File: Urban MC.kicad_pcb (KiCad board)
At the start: 4 copper layers, 166.4 x 125.1 mm, 78 parts, among them J1 Conn_01x02, J2 Conn_01x02, J3 Conn_01x03, J4 Conn_01x02, Q1 IQE022N06LM5CGSCATMA1, Q10 IQE022N06LM5CGSCATMA1, Q11 IQE022N06LM5CGSCATMA1, Q12 IQE022N06LM5CGSCATMA1, Q13 IQE022N06LM5CGSCATMA1, Q14 IQE022N06LM5CGSCATMA1, Q15 IQE022N06LM5CGSCATMA1, Q16 IQE022N06LM5CGSCATMA1, Q17 IQE022N06LM5CGSCATMA1, Q18 IQE022N06LM5CGSCATMA1, Q19 IQE022N06LM5CGSCATMA1, Q2 IQE022N06LM5CGSCATMA1, Q20 IQE022N06LM5CGSCATMA1, Q21 IQE022N06LM5CGSCATMA1, Q22 IQE022N06LM5CGSCATMA1, Q23 IQE022N06LM5CGSCATMA1, Q24 IQE022N06LM5CGSCATMA1, Q3 IQE022N06LM5CGSCATMA1, Q4 IQE022N06LM5CGSCATMA1, Q5 IQE022N06LM5CGSCATMA1, Q6 IQE022N06LM5CGSCATMA1, Q7 IQE022N06LM5CGSCATMA1, Q8 IQE022N06LM5CGSCATMA1, Q9 IQE022N06LM5CGSCATMA1, SW1 CAN_TERM, SW2 SW_Push, U1 MCP2561/2, U2 MCP4725, U3 MCP2515-xSO, Y1 8MHz

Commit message: post design review
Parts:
- moved C10 0.26 mm to (206.0, 89.9)
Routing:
- net GND: track 221.0 -> 179.9 mm, vias 94 -> 92
- net +12V: track 140.8 -> 100.8 mm, vias 2 -> 3
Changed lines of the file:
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@@
 	(footprint "Capacitor_SMD:C_2220_5750Metric"
 		(layer "F.Cu")
-		(at 205.994 90.18 90)
+		(at 205.994 89.916 90)
 		(descr "Capacitor SMD 2220 (5750 Metric), square (rectangular) end terminal, IPC-7351 nominal, (Body size from: http://datasheets.avx.com/AVX-HV_MLCC.pdf), generated with kicad-footprint-generator")
 		(tags "capacitor")
@@
 	)
 	(segment
-		(start 130.81 91.44)
-		(end 128.778 89.408)
-		(width 0.25)
-		(layer "F.Cu")
-		(net 7)
-	)
-	(segment
 		(start 131.572 65.532)
 		(end 132.08 65.532)
@@
 	)
 	(segment
-		(start 132.588 92.964)
-		(end 134.112 92.964)
-		(width 0.25)
-		(layer "F.Cu")
-		(net 7)
-	)
-	(segment
 		(start 121.266474 62.738)
 		(end 121.744737 62.259737)
@@
 	)
 	(segment
-		(start 134.112 92.964)
-		(end 135.382 94.234)
-		(width 0.25)
-		(layer "F.Cu")
-		(net 7)
-	)
-	(segment
 		(start 120.7825 77.47)
 		(end 121.719092 77.47)
@@
 	)
 	(segment
-		(start 128.778 89.408)
-		(end 128.778 79.502)
-		(width 0.25)
-		(layer "F.Cu")
-		(net 7)
-	)
-	(segment
 		(start 153.416 54.102)
 		(end 155.057 52.461)
@@
 	)
 	(via
-		(at 128.778 79.502)
-		(size 0.8)
-		(drill 0.4)
-		(layers "F.Cu" "B.Cu")
-		(net 7)
-	)
-	(via
 		(at 222.504 56.642)
 		(size 0.8)
@@
 	)
 	(via
-		(at 135.382 94.234)
-		(size 0.8)
-		(drill 0.4)
-		(layers "F.Cu" "B.Cu")
-		(net 7)
-	)
-	(via
 		(at 221.742 129.032)
 		(size 0.8)
@@
 	)
 	(segment
-		(start 128.778 79.502)
-		(end 128.27 78.994)
-		(width 0.25)
-		(layer "B.Cu")
-		(net 7)
-	)
-	(segment
 		(start 141.988792 125.476)
 		(end 154.94 125.476)
@@
 	)
 	(segment
-		(start 151.892 94.234)
-		(end 156.718 89.408)
-		(width 0.25)
-		(layer "B.Cu")
-		(net 7)
-	)
-	(segment
 		(start 154.94 125.476)
 		(end 155.702 126.238)
@@
 	)
 	(segment
-		(start 128.27 78.994)
-		(end 127.254 78.994)
-		(width 0.25)
-		(layer "B.Cu")
-		(net 7)
-	)
-	(segment
 		(start 124.9895 65.8075)
 		(end 124.9895 63.7755)
@@
 	)
 	(segment
-		(start 135.382 94.234)
-		(end 151.892 94.234)
-		(width 0.25)
-		(layer "B.Cu")
-		(net 7)
-	)
-	(segment
 		(start 124.9895 63.7755)
 		(end 123.444 62.23)
@@
 	)
 	(via
-		(at 153.924 122.174)
+		(at 134.112 88.9)
 		(size 0.8)
 		(drill 0.4)
@@
 		(net 21)
 	)
-	(segment
-		(start 139.192 88.9)
-		(end 141.224 90.932)
-		(width 1.34)
-		(layer "In2.Cu")
-		(net 21)
-	)
-	(segment
-		(start 141.224 90.932)
-		(end 141.224 120.414052)
-		(width 1.34)
-		(layer "In2.Cu")
+	(via
+		(at 153.924 122.174)
+		(size 0.8)
+		(drill 0.4)
+		(layers "F.Cu" "B.Cu")
 		(net 21)
 	)
@@
 	)
 	(segment
-		(start 144.253948 123.444)
-		(end 152.654 123.444)
+		(start 134.112 88.9)
+		(end 139.192 88.9)
 		(width 1.34)
 		(layer "In2.Cu")
@@
 	)
 	(segment
-		(start 141.224 120.414052)
-		(end 144.253948 123.444)
+		(start 144.253948 123.444)
+		(end 152.654 123.444)
 		(width 1.34)
 		(layer "In2.Cu")
@@
 	)
 	(segment
-		(start 130.81 88.9)
-		(end 139.192 88.9)
-		(width 1.34)
-		(layer "In2.Cu")
-		(net 21)
-	)
-	(segment
 		(start 153.416 88.9)
 		(end 154.432 87.884)
@@
 		(polygon
 			(pts
-				(xy 171.972957 71.891994) (xy 239.536957 72.145994) (xy 239.536957 79.003994) (xy 259.073585 79.003994)
-				(xy 259.073585 93.989994) (xy 239.790957 93.989994) (xy 239.790957 87.701768) (xy 209.162714 87.701768)
-				(xy 209.162714 88.336768) (xy 171.97264 88.299721) (xy 171.941329 83.243024)
+				(xy 171.958 71.882) (xy 239.522 71.882) (xy 239.536957 79.003994) (xy 259.073585 78.994) (xy 259.073585 93.989994)
+				(xy 239.790957 93.989994) (xy 239.790957 87.701768) (xy 209.162714 87.701768) (xy 209.162714 88.336768)
+				(xy 171.97264 88.299721) (xy 171.941329 83.243024)
 			)
 		)
@@
 		(polygon
 			(pts
-				(xy 170.942 90.424) (xy 199.644 90.424) (xy 199.644 106.172) (xy 167.132 106.172) (xy 167.132 112.268)
-				(xy 152.4 112.268) (xy 152.146 134.62) (xy 169.672 134.62) (xy 169.672 127) (xy 199.898 127) (xy 199.898 142.494)
+				(xy 170.942 90.424) (xy 199.644 90.424) (xy 199.644 106.172) (xy 170.434 106.172) (xy 170.434 112.268)
+				(xy 152.4 112.268) (xy 152.4 134.62) (xy 169.672 134.62) (xy 169.672 127) (xy 199.898 127) (xy 199.898 142.494)
 				(xy 240.538 142.494) (xy 240.538 136.652) (xy 259.08 136.652) (xy 259.08 153.67) (xy 136.435317 153.67)
 				(xy 136.525 59.944) (xy 171.45 59.944) (xy 171.45 54.61) (xy 199.898 54.61) (xy 199.898 71.12) (xy 171.196 71.12)
@@
 		(polygon
 			(pts
-				(xy 200.914 89.662) (xy 213.049576 89.684724) (xy 213.042396 88.101473) (xy 239.035372 88.072385)
-				(xy 239.035372 105.918) (xy 200.914 105.918)
+				(xy 200.66 91.186) (xy 213.106 91.186) (xy 213.106 89.662) (xy 239.014 89.662) (xy 239.035372 105.918)
+				(xy 200.66 105.918)
 			)
 		)
@@
 		(polygon
 			(pts
-				(xy 171.958 71.882) (xy 239.522 72.136) (xy 239.522 78.994) (xy 259.058628 78.994) (xy 259.058628 93.98)
+				(xy 171.958 71.882) (xy 239.522 71.882) (xy 239.522 78.994) (xy 259.058628 78.994) (xy 259.058628 93.98)
 				(xy 239.776 93.98) (xy 239.776 87.691774) (xy 209.147757 87.691774) (xy 209.147757 88.326774) (xy 171.957683 88.289727)
 				(xy 171.926372 83.23303)
@@
 		(polygon
 			(pts
-				(xy 170.942 90.424) (xy 199.644 90.424) (xy 199.644 106.172) (xy 167.132 106.172) (xy 167.132 112.268)
-				(xy 152.4 112.268) (xy 152.146 134.62) (xy 169.672 134.62) (xy 169.672 127) (xy 199.898 127) (xy 199.898 142.494)
+				(xy 170.942 90.424) (xy 199.644 90.424) (xy 199.644 106.172) (xy 170.434 106.172) (xy 170.434 112.268)
+				(xy 152.4 112.268) (xy 152.4 134.62) (xy 169.672 134.62) (xy 169.672 127) (xy 199.898 127) (xy 199.898 142.494)
 				(xy 240.538 142.494) (xy 240.538 136.652) (xy 259.08 136.652) (xy 259.08 153.67) (xy 136.435317 153.67)
 				(xy 136.525 59.944) (xy 171.45 59.944) (xy 171.45 54.61) (xy 199.898 54.61) (xy 199.898 71.12) (xy 171.196 71.12)

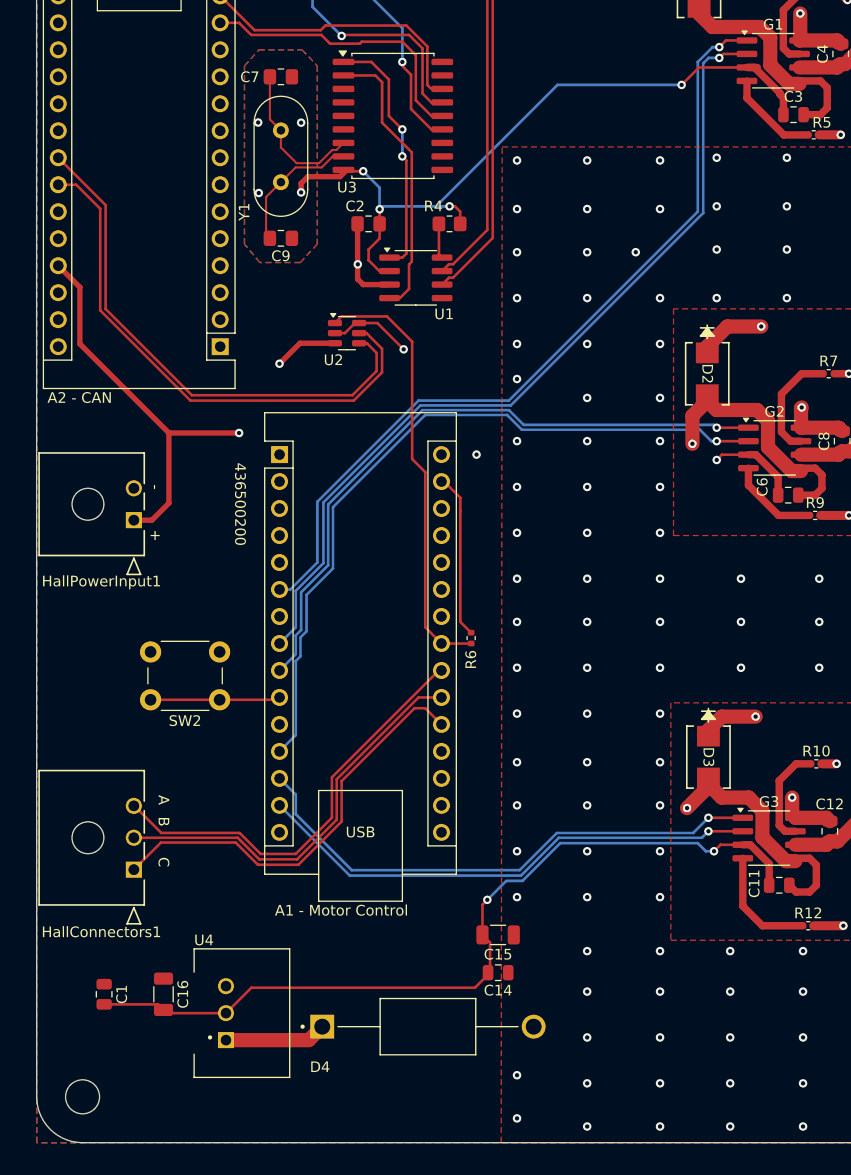
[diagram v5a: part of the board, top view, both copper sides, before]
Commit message: grounding components with vias instead of long traces, 5V filled zone and MCP4725 complementary components
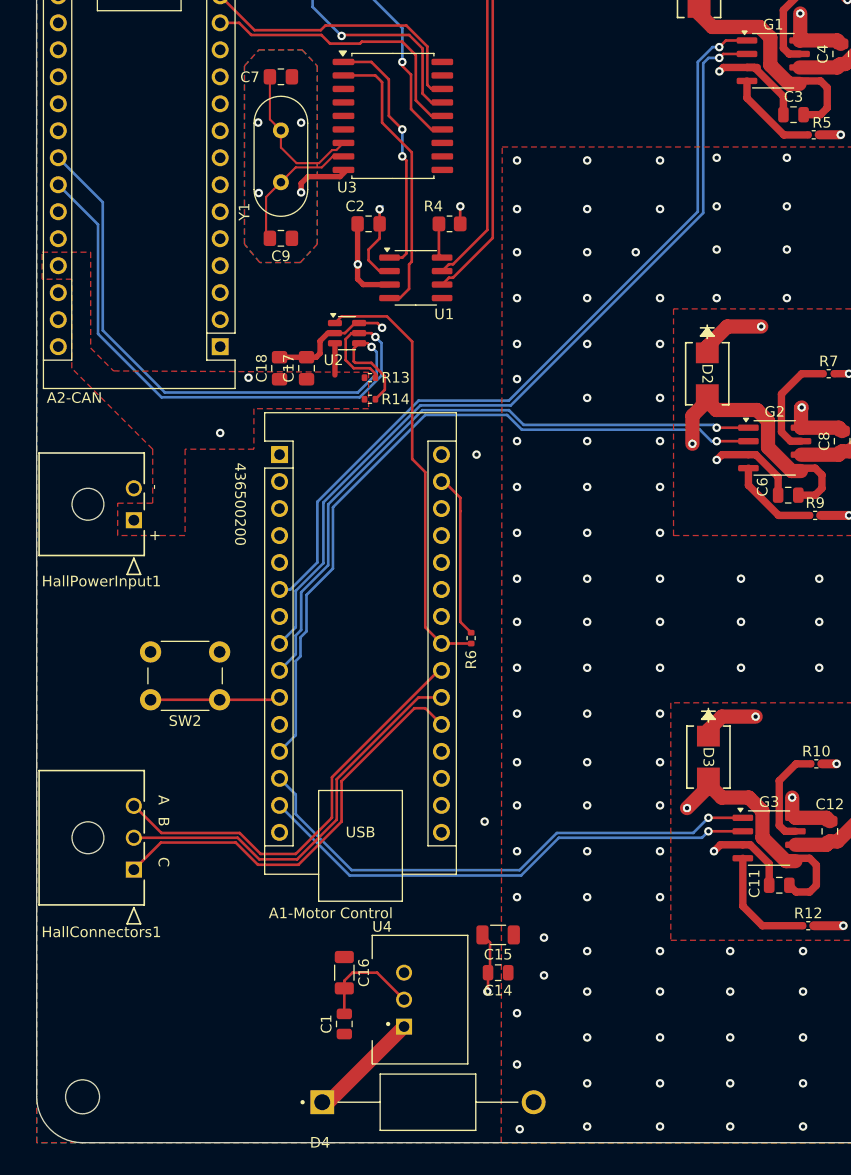
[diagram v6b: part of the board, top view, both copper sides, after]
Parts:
- removed A1 - Motor Control: Arduino_Nano_v2.x, Module:Arduino_Nano
- removed A2 - CAN: Arduino_Nano_v2.x, Module:Arduino_Nano
- added A1-Motor Control: Arduino_Nano_v2.x, Module:Arduino_Nano, F.Cu at (115.6, 88.9)
- added A2-CAN: Arduino_Nano_v2.x, Module:Arduino_Nano, F.Cu at (110.0, 78.7)
- added C17: 0.1uF, Capacitor_SMD:C_0805_2012Metric_Pad1.18x1.45mm_HandSolder, F.Cu at (118.1, 80.8)
- added C18: 10uF, Capacitor_SMD:C_0805_2012Metric_Pad1.18x1.45mm_HandSolder, F.Cu at (115.6, 80.8)
- added R13: 10K, Resistor_SMD:R_0402_1005Metric, F.Cu at (124.1, 81.7)
- added R14: 10K, Resistor_SMD:R_0402_1005Metric, F.Cu at (124.1, 83.7)
- moved C1 22.8 mm to (121.7, 142.5), turned to 90 degrees
- moved C16 17.1 mm to (121.7, 137.7)
- moved U4 16.8 mm to (129.5, 140.0)
- moved D4 7.11 mm to (129.5, 149.9)
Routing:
- net GND: track 179.9 -> 85.7 mm, vias 92 -> 91
- net +5V: track 97.0 -> 53.3 mm
- net +12V: track 100.8 -> 110.2 mm, vias 3 -> 4
- net /A4: track 49.6 -> 58.9 mm, vias 0 -> 1
- net /A5: track 50.6 -> 58.6 mm, vias 0 -> 1
- net Net-(U4-VIN): track 9.59 -> 10.6 mm
- net +48V: vias 180 -> 183
- added copper zone on F.Cu, net +5V
